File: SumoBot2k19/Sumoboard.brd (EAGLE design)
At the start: 80 x 50 mm, 37 parts

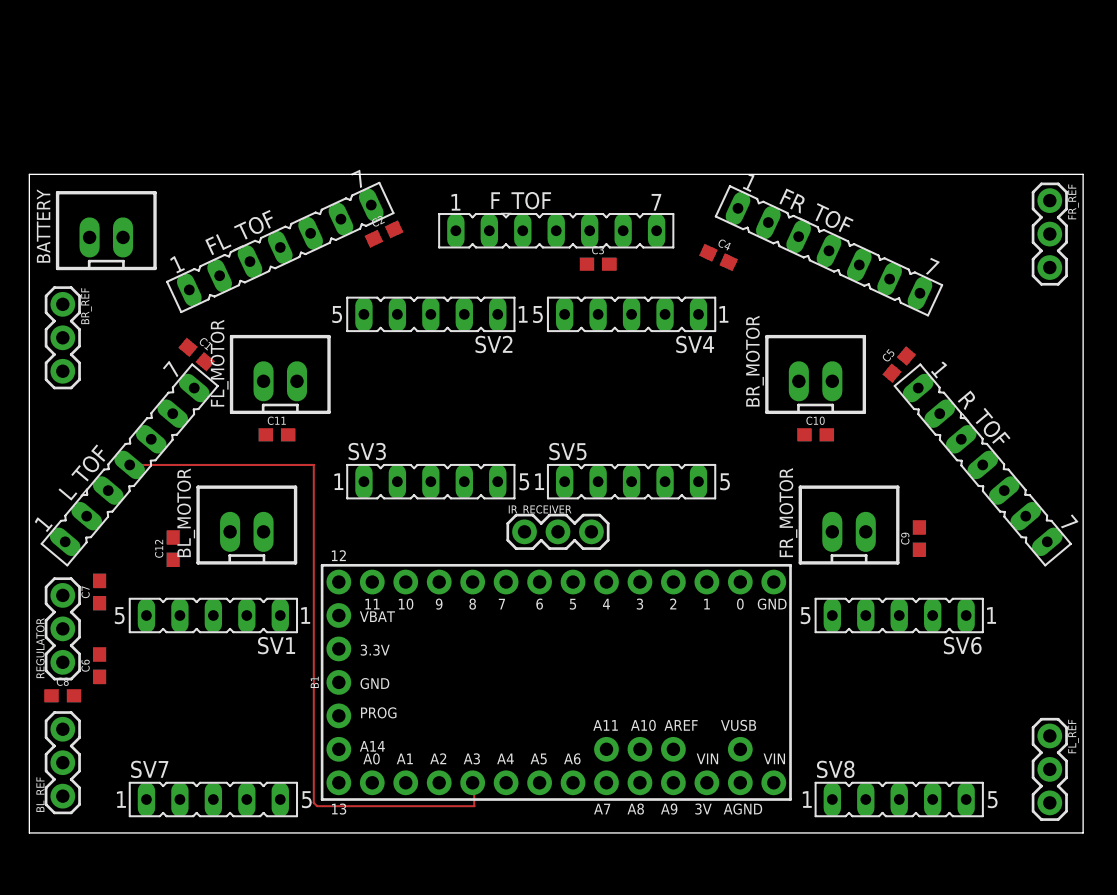
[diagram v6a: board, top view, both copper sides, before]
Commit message: began routing on PCB, moved components around for extra clarity, learned how to align things
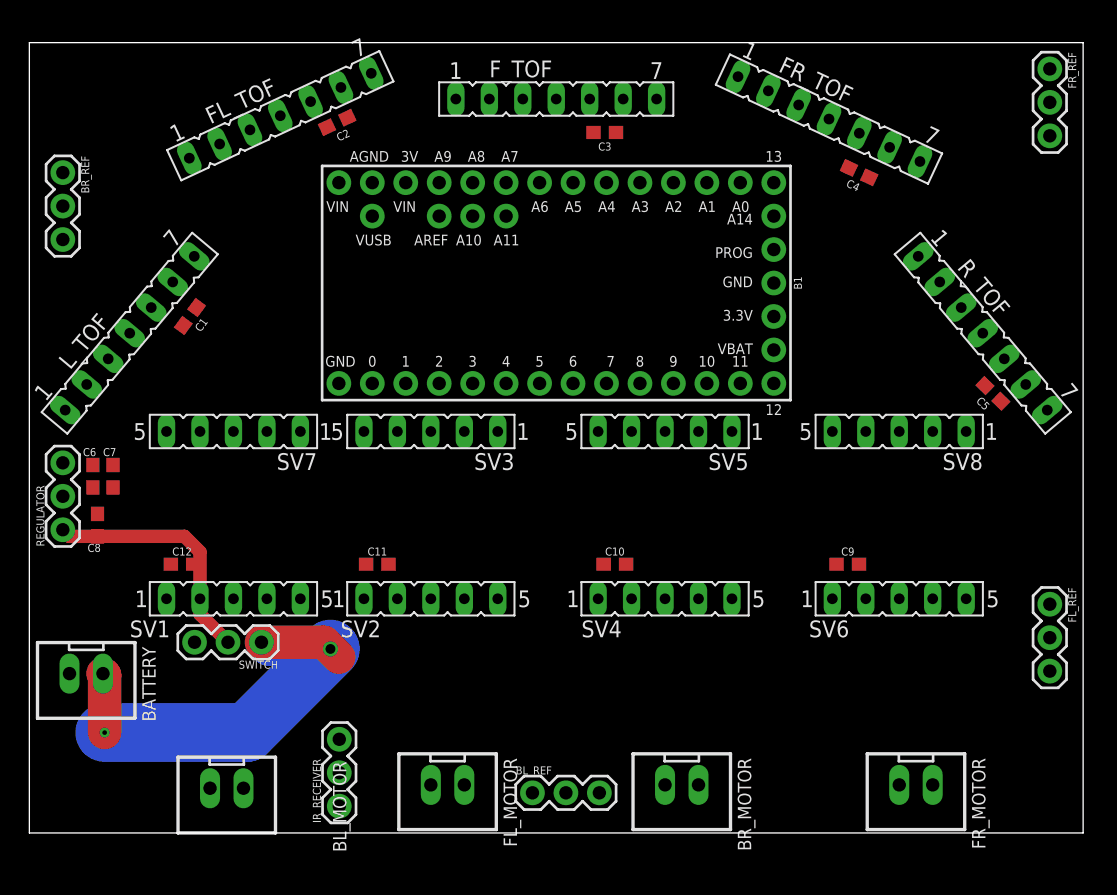
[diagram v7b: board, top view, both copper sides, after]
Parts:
- added SWITCH: (no value), SparkFun-Connectors:1X03
- moved BL_REF 35.7 mm to (38.2, 3.05), turned to 0 degrees
- moved FL_MOTOR 33.2 mm to (31.8, 3.65), turned to 180 degrees
- moved BATTERY 33.1 mm to (4.32, 12.1), turned to 180 degrees
- moved BR_MOTOR 32.3 mm to (49.5, 3.65), turned to 180 degrees
- moved B1 30.3 mm to (40.0, 41.8), turned to 270 degrees
- moved SV7 28.0 mm to (15.5, 30.5), turned to 180 degrees
- moved SV8 27.9 mm to (66.0, 30.5), turned to 180 degrees
- moved IR_RECEIVER 25.1 mm to (23.5, 2.03), turned to 90 degrees
- moved SV4 21.7 mm to (48.3, 17.8), turned to 0 degrees
- moved SV2 21.6 mm to (30.5, 17.8), turned to 0 degrees
- moved FR_MOTOR 19.9 mm to (67.3, 3.65), turned to 180 degrees
- moved BL_MOTOR 19.5 mm to (15.0, 3.40), turned to 180 degrees
- moved C10 18.1 mm to (44.5, 20.4), turned to 180 degrees
- moved C6 14.4 mm to (4.83, 27.1), turned to 270 degrees
- moved C8 13.2 mm to (5.17, 23.4), turned to 270 degrees
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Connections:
- removed net VIN1: C10.1
- removed net VIN2: C11.1
- removed net VIN3: C12.1
- net LEFT_DIR: now also B1.9; no longer B1.2
- net LEFT_PWM: now also B1.8; no longer B1.3
- net RIGHT_DIR: now also B1.3; no longer B1.8
- net RIGHT_PWM: now also B1.2; no longer B1.9
- net VBAT: now also BATTERY.1, SWITCH.1
- net VIN: now also C10.1, C11.1, C12.1, SWITCH.2; no longer BATTERY.1
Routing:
- net SDA: track 53.8 -> 0.00 mm
- net VBAT: track 0.00 -> 36.1 mm, vias 0 -> 2
- net VIN: track 0.00 -> 18.9 mm
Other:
- board size 80 x 50 mm -> 80 x 60 mm

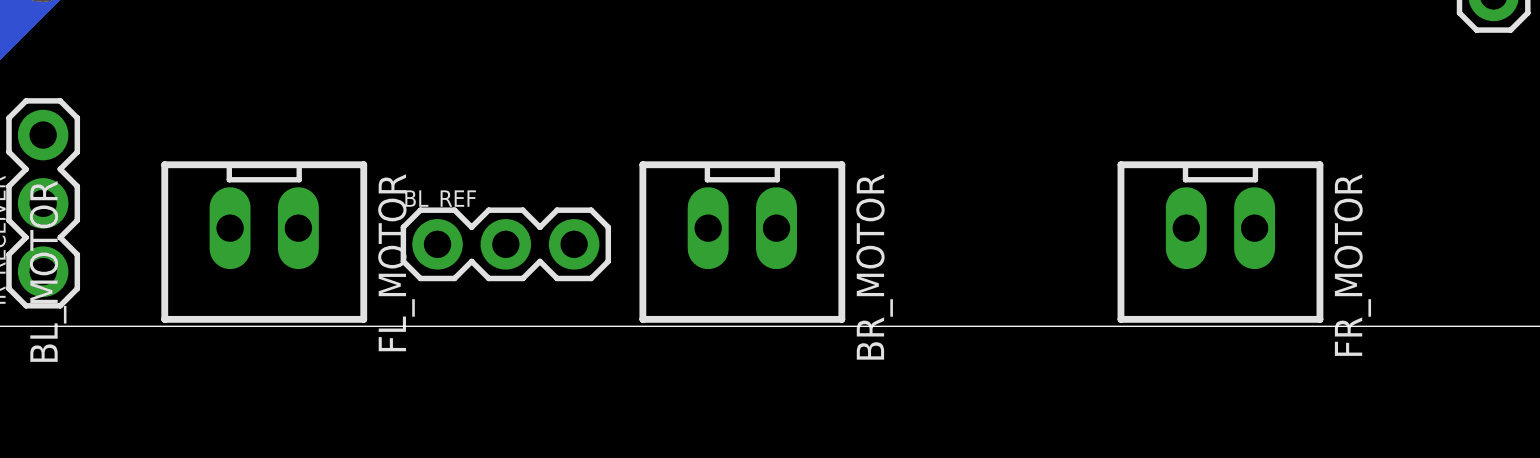
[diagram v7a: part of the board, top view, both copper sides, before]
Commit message: trying to change the left/right pwm/direction pins
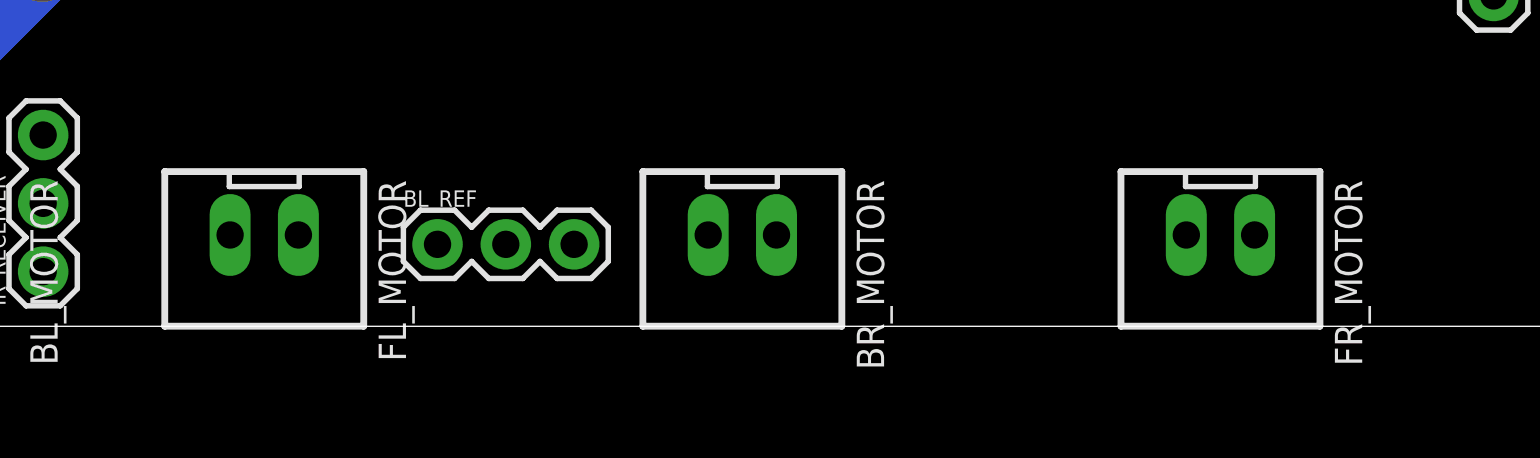
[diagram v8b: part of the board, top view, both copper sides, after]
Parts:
- moved BR_MOTOR 0.25 mm to (49.5, 3.40)
- moved FL_MOTOR 0.25 mm to (31.8, 3.40)
- moved FR_MOTOR 0.25 mm to (67.3, 3.40)
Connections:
- new net RIGHT: B1.13
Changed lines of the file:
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@@
 <attribute name="VALUE" x="36.92400625" y="1.016" size="0.6096" layer="27" font="vector" ratio="20"/>
 </element>
-<element name="BR_MOTOR" library="Rembrandt Electronics - JST XH Connectors v1-0" package="JST-XH-02-PACKAGE-LONG-PAD" value="JST-XH-02-PIN-LONG-PAD" x="49.53" y="3.65000625" smashed="yes" rot="R180">
-<attribute name="NAME" x="53.785" y="5.69000625" size="1.016" layer="25" ratio="10" rot="R270"/>
-<attribute name="VALUE" x="52.8325" y="-0.24249375" size="1.016" layer="27" ratio="10" rot="R180"/>
+<element name="BR_MOTOR" library="Rembrandt Electronics - JST XH Connectors v1-0" package="JST-XH-02-PACKAGE-LONG-PAD" value="JST-XH-02-PIN-LONG-PAD" x="49.53" y="3.39600625" smashed="yes" rot="R180">
+<attribute name="NAME" x="53.785" y="5.43600625" size="1.016" layer="25" ratio="10" rot="R270"/>
+<attribute name="VALUE" x="52.8325" y="-0.49649375" size="1.016" layer="27" ratio="10" rot="R180"/>
 </element>
 <element name="BR_REF" library="SparkFun-Connectors" library_urn="urn:adsk.eagle:library:513" package="1X03" package3d_urn="urn:adsk.eagle:package:38063/1" value="" x="2.54" y="50.13200625" smashed="yes" rot="R270">
@@
 <attribute name="VALUE" x="62.13599375" y="21.161996875" size="0.6096" layer="27" font="vector" ratio="20" rot="R180" align="top-center"/>
 </element>
-<element name="FL_MOTOR" library="Rembrandt Electronics - JST XH Connectors v1-0" package="JST-XH-02-PACKAGE-LONG-PAD" value="JST-XH-02-PIN-LONG-PAD" x="31.75" y="3.65000625" smashed="yes" rot="R180">
-<attribute name="NAME" x="36.005" y="5.69000625" size="1.016" layer="25" ratio="10" rot="R270"/>
-<attribute name="VALUE" x="35.0525" y="-0.24249375" size="1.016" layer="27" ratio="10" rot="R180"/>
+<element name="FL_MOTOR" library="Rembrandt Electronics - JST XH Connectors v1-0" package="JST-XH-02-PACKAGE-LONG-PAD" value="JST-XH-02-PIN-LONG-PAD" x="31.75" y="3.39600625" smashed="yes" rot="R180">
+<attribute name="NAME" x="36.005" y="5.43600625" size="1.016" layer="25" ratio="10" rot="R270"/>
+<attribute name="VALUE" x="35.0525" y="-0.49649375" size="1.016" layer="27" ratio="10" rot="R180"/>
 </element>
 <element name="FL_REF" library="SparkFun-Connectors" library_urn="urn:adsk.eagle:library:513" package="1X03" package3d_urn="urn:adsk.eagle:package:38063/1" value="" x="77.47" y="17.36600625" smashed="yes" rot="R270">
@@
 <attribute name="VALUE" x="13.3784" y="48.582328125" size="1.27" layer="27" ratio="10" rot="R25"/>
 </element>
-<element name="FR_MOTOR" library="Rembrandt Electronics - JST XH Connectors v1-0" package="JST-XH-02-PACKAGE-LONG-PAD" value="JST-XH-02-PIN-LONG-PAD" x="67.31" y="3.65000625" smashed="yes" rot="R180">
-<attribute name="NAME" x="71.565" y="5.69000625" size="1.016" layer="25" ratio="10" rot="R270"/>
-<attribute name="VALUE" x="70.6125" y="-0.24249375" size="1.016" layer="27" ratio="10" rot="R180"/>
+<element name="FR_MOTOR" library="Rembrandt Electronics - JST XH Connectors v1-0" package="JST-XH-02-PACKAGE-LONG-PAD" value="JST-XH-02-PIN-LONG-PAD" x="67.31" y="3.39600625" smashed="yes" rot="R180">
+<attribute name="NAME" x="71.565" y="5.43600625" size="1.016" layer="25" ratio="10" rot="R270"/>
+<attribute name="VALUE" x="70.6125" y="-0.49649375" size="1.016" layer="27" ratio="10" rot="R180"/>
 </element>
 <element name="FR_REF" library="SparkFun-Connectors" library_urn="urn:adsk.eagle:library:513" package="1X03" package3d_urn="urn:adsk.eagle:package:38063/1" value="" x="77.47" y="58.00600625" smashed="yes" rot="R270">
@@
 <contactref element="SV4" pad="4"/>
 <contactref element="BR_MOTOR" pad="1"/>
-<wire x1="50.8" y1="3.65000625" x2="50.8" y2="17.78" width="0" layer="19" extent="1-1"/>
+<wire x1="50.8" y1="3.39600625" x2="50.8" y2="17.78" width="0" layer="19" extent="1-1"/>
 </signal>
 <signal name="N$4">
 <contactref element="BR_MOTOR" pad="2"/>
 <contactref element="SV4" pad="3"/>
-<wire x1="48.26" y1="3.65000625" x2="48.26" y2="17.78" width="0" layer="19" extent="1-1"/>
+<wire x1="48.26" y1="3.39600625" x2="48.26" y2="17.78" width="0" layer="19" extent="1-1"/>
 </signal>
 <signal name="N$5">
 <contactref element="SV2" pad="4"/>
 <contactref element="FL_MOTOR" pad="1"/>
-<wire x1="33.02" y1="3.65000625" x2="33.02" y2="17.78" width="0" layer="19" extent="1-1"/>
+<wire x1="33.02" y1="3.39600625" x2="33.02" y2="17.78" width="0" layer="19" extent="1-1"/>
 </signal>
 <signal name="N$6">
 <contactref element="FL_MOTOR" pad="2"/>
 <contactref element="SV2" pad="3"/>
-<wire x1="30.48" y1="3.65000625" x2="30.48" y2="17.78" width="0" layer="19" extent="1-1"/>
+<wire x1="30.48" y1="3.39600625" x2="30.48" y2="17.78" width="0" layer="19" extent="1-1"/>
 </signal>
 <signal name="N$7">
 <contactref element="SV6" pad="4"/>
 <contactref element="FR_MOTOR" pad="1"/>
-<wire x1="68.58" y1="3.65000625" x2="68.58" y2="17.78" width="0" layer="19" extent="1-1"/>
+<wire x1="68.58" y1="3.39600625" x2="68.58" y2="17.78" width="0" layer="19" extent="1-1"/>
 </signal>
 <signal name="N$8">
 <contactref element="SV6" pad="3"/>
 <contactref element="FR_MOTOR" pad="2"/>
-<wire x1="66.04" y1="3.65000625" x2="66.04" y2="17.78" width="0" layer="19" extent="1-1"/>
+<wire x1="66.04" y1="3.39600625" x2="66.04" y2="17.78" width="0" layer="19" extent="1-1"/>
+</signal>
+<signal name="RIGHT">
+<contactref element="B1" pad="13"/>
 </signal>
 </signals>
